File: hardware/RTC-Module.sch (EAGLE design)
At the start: 14 parts, among them Q1 32.768kHz, U1 DS1307

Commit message: Removed Sparkfun web logo
Just not enough room for it. The SF flame should suffice.
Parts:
- removed LOGO2: SFE_LOGO_NAME_FLAME.1_INCH, SparkFun-Aesthetics:SFE_LOGO_NAME_FLAME.1_INCH
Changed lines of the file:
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@@
 <part name="FRAME2" library="SparkFun-Aesthetics" deviceset="FRAME-LETTER" device=""/>
 <part name="LOGO1" library="SparkFun-Aesthetics" deviceset="OSHW-LOGO" device="S"/>
-<part name="LOGO2" library="SparkFun-Aesthetics" deviceset="SFE_LOGO_NAME_FLAME" device=".1_INCH"/>
 </parts>
 <sheets>
@@
 <instance part="FRAME2" gate="G$2" x="147.32" y="0"/>
 <instance part="LOGO1" gate="G$1" x="215.9" y="48.26"/>
-<instance part="LOGO2" gate="G$1" x="88.9" y="2.54"/>
 </instances>
 <busses>

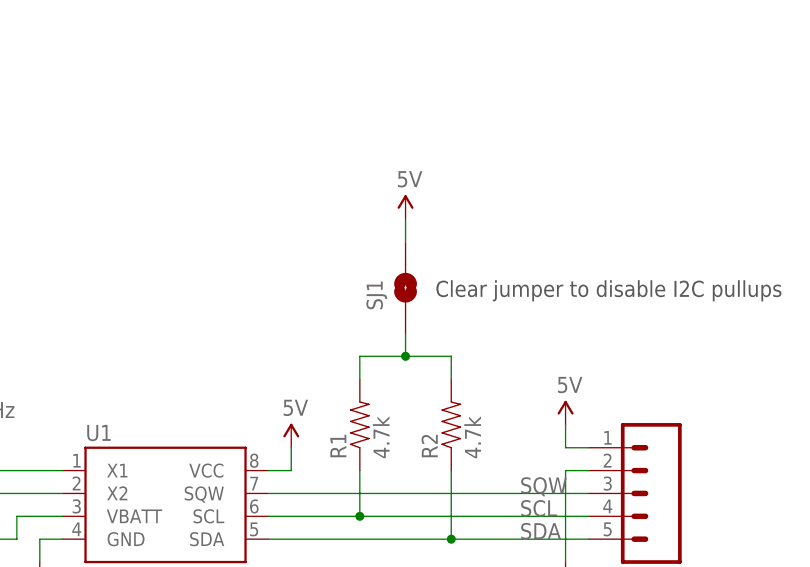
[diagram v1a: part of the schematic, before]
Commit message: Fixed I2C jumper. Silk mods. Removed restrict polygon.
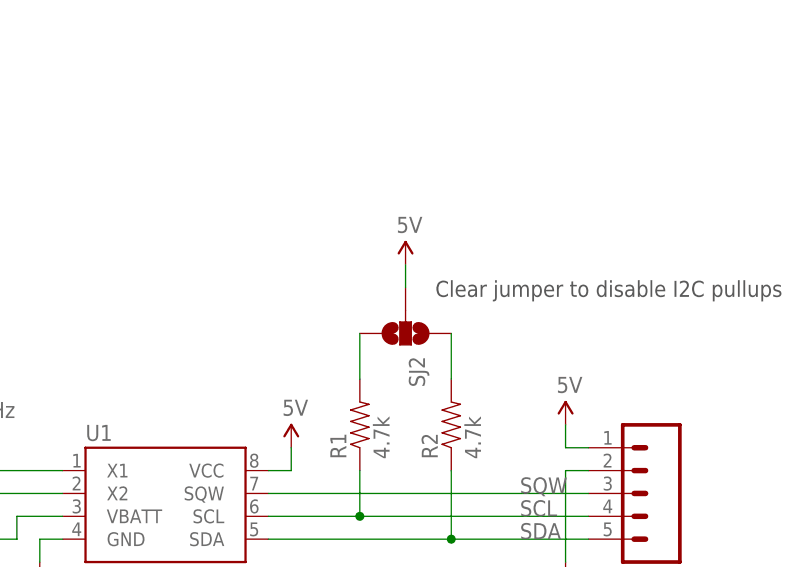
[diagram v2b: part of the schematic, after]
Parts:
- removed SJ1: SOLDERJUMPERNC, SparkFun-Passives:SOLDERJUMPERNC
- added SJ2: (no value), SparkFun-Passives:SOLDERJUMPER_2WAYPASTE1&2&3
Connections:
- removed net N$3: R1.2, R2.2, SJ1.1
- new net N$5: R1.2, SJ2.3
- new net N$6: R2.2, SJ2.1
- net 5V: now also SJ2.2; no longer SJ1.2
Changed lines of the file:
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@@
 <part name="R1" library="SparkFun-Resistors" deviceset="4.7KOHM1/10W1%(0603)" device="" value="4.7k"/>
 <part name="R2" library="SparkFun-Resistors" deviceset="4.7KOHM1/10W1%(0603)" device="" value="4.7k"/>
-<part name="SJ1" library="SparkFun-Passives" deviceset="SOLDERJUMPER" device="NC" value=""/>
 <part name="GND4" library="SparkFun" deviceset="GND" device=""/>
 <part name="SUPPLY1" library="SparkFun-Aesthetics" deviceset="5V" device=""/>
@@
 <part name="FRAME2" library="SparkFun-Aesthetics" deviceset="FRAME-LETTER" device=""/>
 <part name="LOGO1" library="SparkFun-Aesthetics" deviceset="OSHW-LOGO" device="S"/>
+<part name="SJ2" library="SparkFun-Passives" deviceset="SOLDERJUMPER_2WAY" device="PASTE1&amp;2&amp;3"/>
 </parts>
 <sheets>
@@
 <instance part="R1" gate="G$1" x="129.54" y="109.22" rot="R90"/>
 <instance part="R2" gate="G$1" x="139.7" y="109.22" rot="R90"/>
-<instance part="SJ1" gate="1" x="134.62" y="124.46" rot="R90"/>
 <instance part="GND4" gate="1" x="152.4" y="91.44"/>
 <instance part="SUPPLY1" gate="G$1" x="152.4" y="109.22"/>
 <instance part="SUPPLY2" gate="G$1" x="121.92" y="106.68"/>
-<instance part="SUPPLY3" gate="G$1" x="134.62" y="132.08"/>
+<instance part="SUPPLY3" gate="G$1" x="134.62" y="127"/>
 <instance part="SUPPLY4" gate="G$1" x="63.5" y="101.6"/>
 <instance part="FRAME2" gate="G$1" x="0" y="0"/>
 <instance part="FRAME2" gate="G$2" x="147.32" y="0"/>
 <instance part="LOGO1" gate="G$1" x="215.9" y="48.26"/>
+<instance part="SJ2" gate="G$1" x="134.62" y="119.38" rot="R270"/>
 </instances>
 <busses>
@@
 </segment>
 </net>
-<net name="N$3" class="0">
-<segment>
-<pinref part="SJ1" gate="1" pin="1"/>
-<wire x1="134.62" y1="119.38" x2="134.62" y2="116.84" width="0.1524" layer="91"/>
-<pinref part="R2" gate="G$1" pin="2"/>
-<wire x1="134.62" y1="116.84" x2="139.7" y2="116.84" width="0.1524" layer="91"/>
-<wire x1="139.7" y1="116.84" x2="139.7" y2="114.3" width="0.1524" layer="91"/>
-<pinref part="R1" gate="G$1" pin="2"/>
-<wire x1="134.62" y1="116.84" x2="129.54" y2="116.84" width="0.1524" layer="91"/>
-<wire x1="129.54" y1="116.84" x2="129.54" y2="114.3" width="0.1524" layer="91"/>
-<junction x="134.62" y="116.84"/>
-</segment>
-</net>
 <net name="5V" class="0">
 <segment>
@@
 </segment>
 <segment>
-<pinref part="SJ1" gate="1" pin="2"/>
-<wire x1="134.62" y1="132.08" x2="134.62" y2="129.54" width="0.1524" layer="91"/>
 <pinref part="SUPPLY3" gate="G$1" pin="5V"/>
+<pinref part="SJ2" gate="G$1" pin="2"/>
+<wire x1="134.62" y1="127" x2="134.62" y2="124.46" width="0.1524" layer="91"/>
 </segment>
 <segment>
@@
 </segment>
 </net>
+<net name="N$5" class="0">
+<segment>
+<pinref part="R1" gate="G$1" pin="2"/>
+<pinref part="SJ2" gate="G$1" pin="3"/>
+<wire x1="129.54" y1="119.38" x2="129.54" y2="114.3" width="0.1524" layer="91"/>
+</segment>
+</net>
+<net name="N$6" class="0">
+<segment>
+<pinref part="R2" gate="G$1" pin="2"/>
+<pinref part="SJ2" gate="G$1" pin="1"/>
+<wire x1="139.7" y1="119.38" x2="139.7" y2="114.3" width="0.1524" layer="91"/>
+</segment>
+</net>

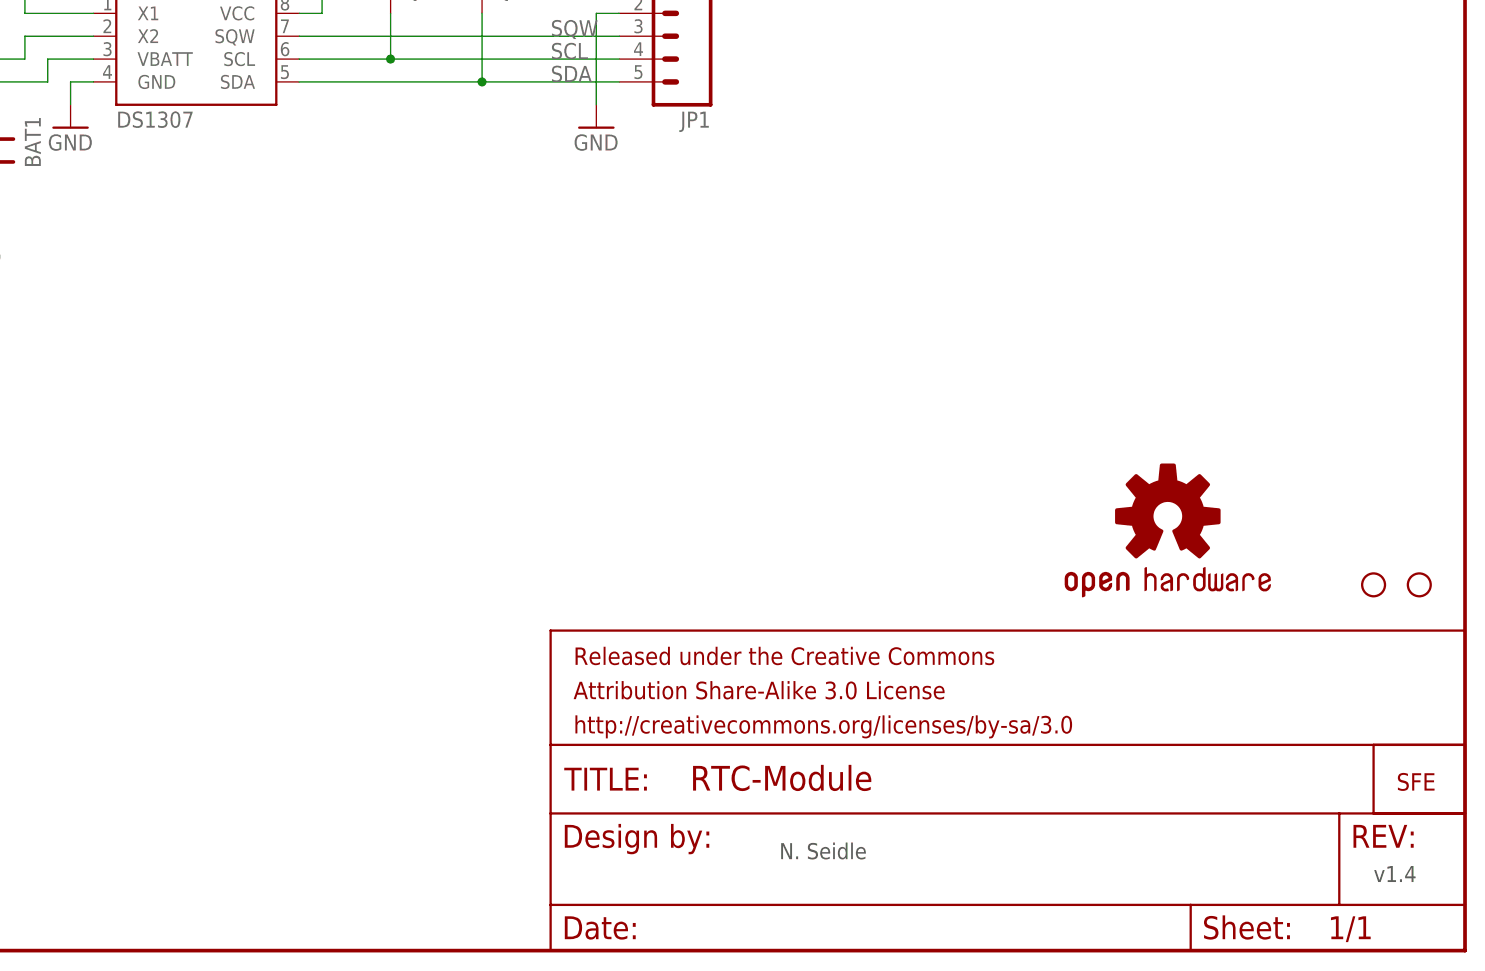
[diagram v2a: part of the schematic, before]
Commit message: Minor fixes
1.) added i2c address to sch
2.) added rev number in bottom copper
3.) updated revision info in sch and brd
4.) moved fiducials to clear drc
5.) cleaned up sda trace a bit
6.) added flame to bottom silk
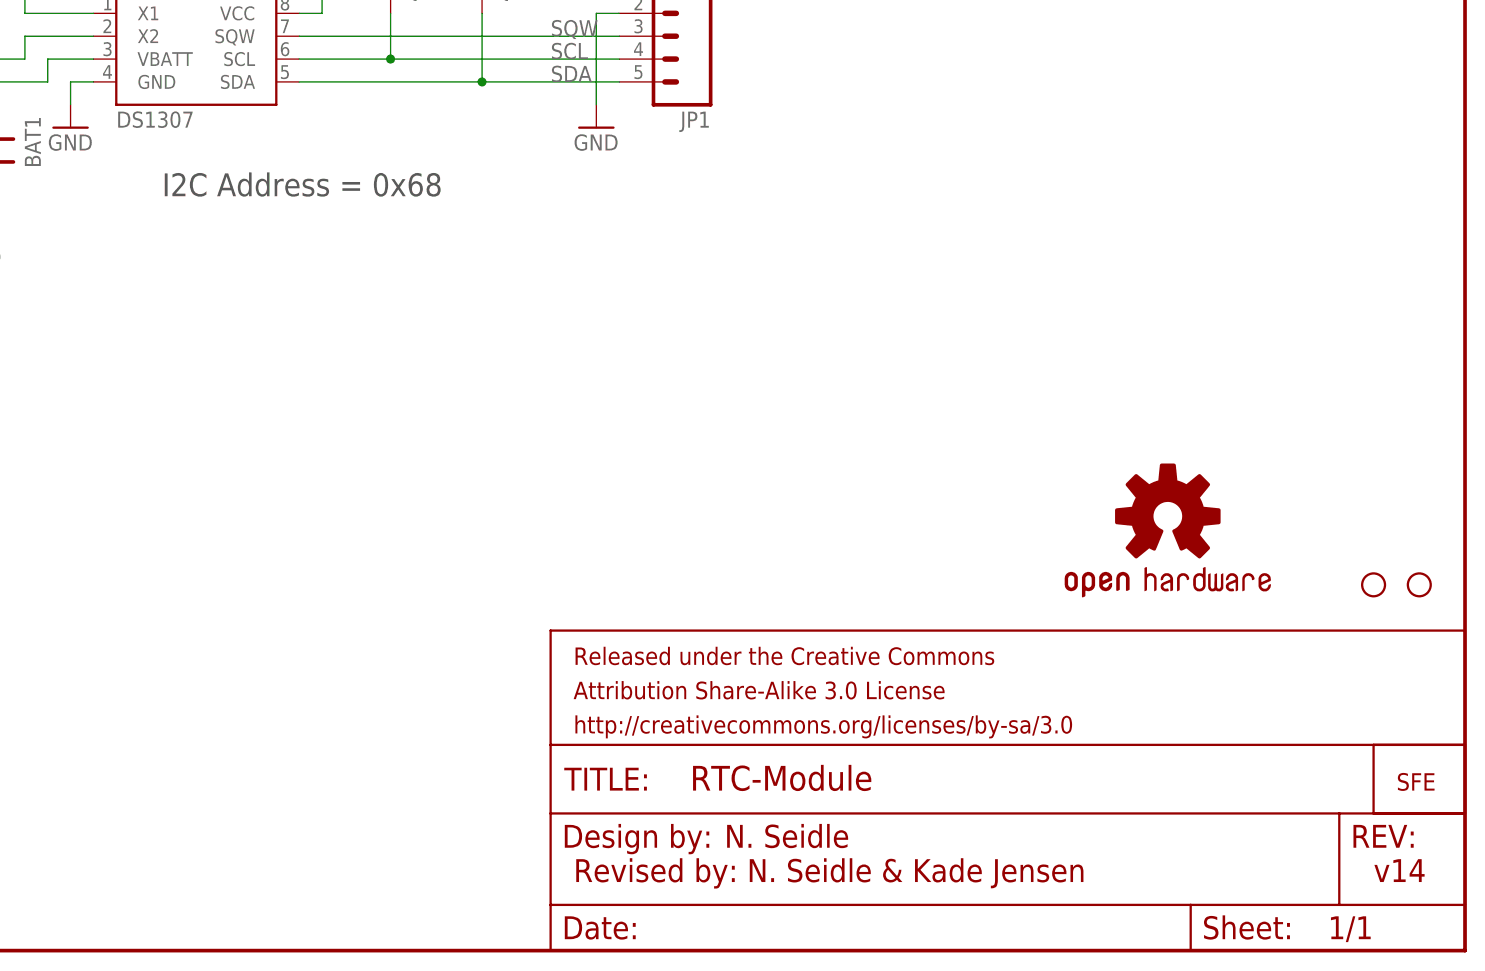
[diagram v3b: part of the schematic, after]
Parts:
- renumbered U$1 to U$2
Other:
- note added: "I2C Address = 0x68"
- note added: "Revised by: N. Seidle & Kade Jensen"
- note added: "v14"
- note removed: "v1.4"
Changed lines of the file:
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@@
 </classes>
 <parts>
-<part name="U$1" library="SparkFun" deviceset="LOGO-SFE" device="SK"/>
+<part name="U$2" library="SparkFun" deviceset="LOGO-SFE" device="SK"/>
 <part name="U$6" library="SparkFun" deviceset="STAND-OFF" device=""/>
 <part name="U$7" library="SparkFun" deviceset="STAND-OFF" device=""/>
@@
 <sheet>
 <plain>
-<text x="238.76" y="7.62" size="1.778" layer="97">v1.4</text>
-<text x="172.72" y="10.16" size="1.778" layer="97">N. Seidle</text>
+<text x="238.76" y="7.62" size="2.54" layer="94">v14</text>
+<text x="166.624" y="11.43" size="2.54" layer="94">N. Seidle</text>
 <text x="137.922" y="123.444" size="1.778" layer="97">Clear jumper to disable I2C pullups</text>
+<text x="149.86" y="7.62" size="2.54" layer="94">Revised by: N. Seidle &amp; Kade Jensen</text>
+<text x="104.14" y="83.82" size="2.54" layer="97">I2C Address = 0x68</text>
 </plain>
 <instances>
-<instance part="U$1" gate="G$1" x="241.3" y="17.78"/>
+<instance part="U$2" gate="G$1" x="241.3" y="17.78"/>
 <instance part="U$6" gate="G$1" x="238.76" y="40.64"/>
 <instance part="U$7" gate="G$1" x="243.84" y="40.64"/>
